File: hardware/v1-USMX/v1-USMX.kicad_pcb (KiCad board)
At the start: 2 copper layers, 91.4 x 48.8 mm, 38 parts, among them IC1 MAX98357AETE+T (L), IC2 MAX98357AETE+T (R), J1 +5v_POWER, J2 Conn_01x04, J3 10118192-0002LF, J4 Serial_Breakout, U1 ESP32-S3-WROOM-1, U2 AZ1084-3.3

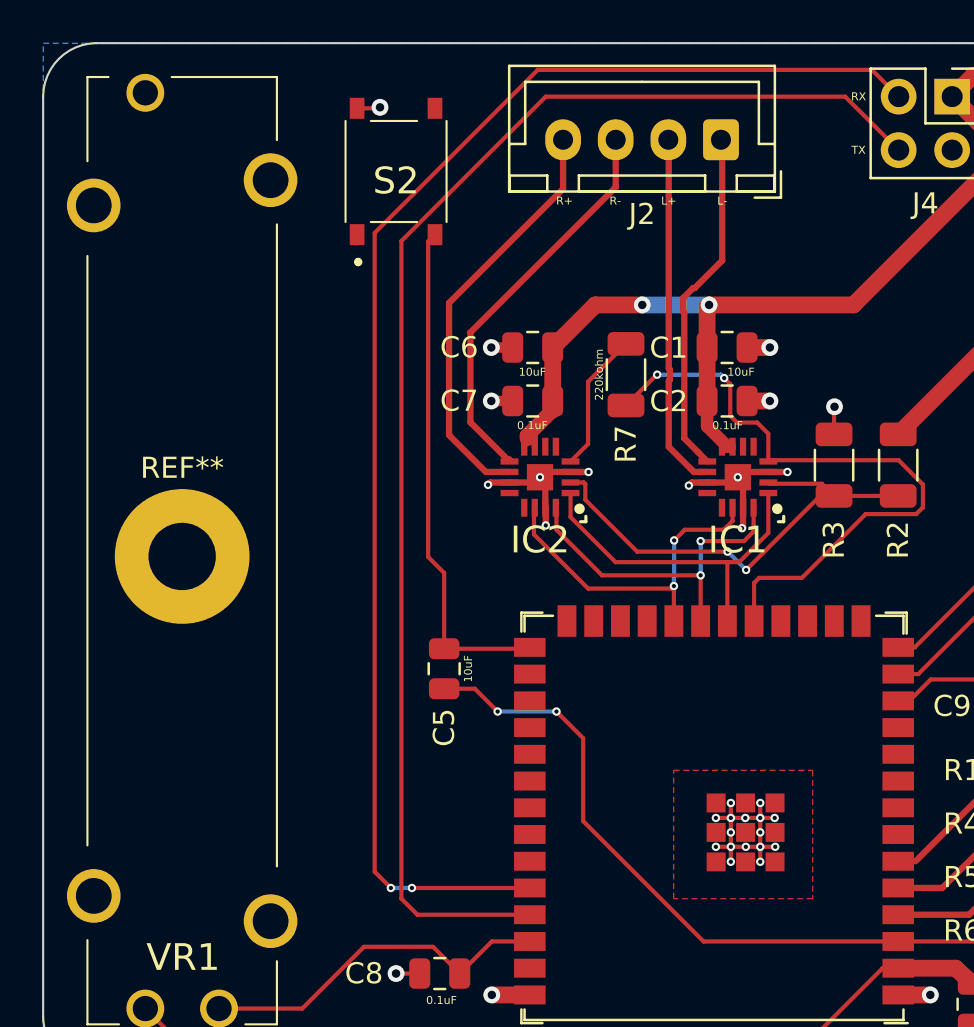
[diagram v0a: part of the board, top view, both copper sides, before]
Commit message: passes all DRC
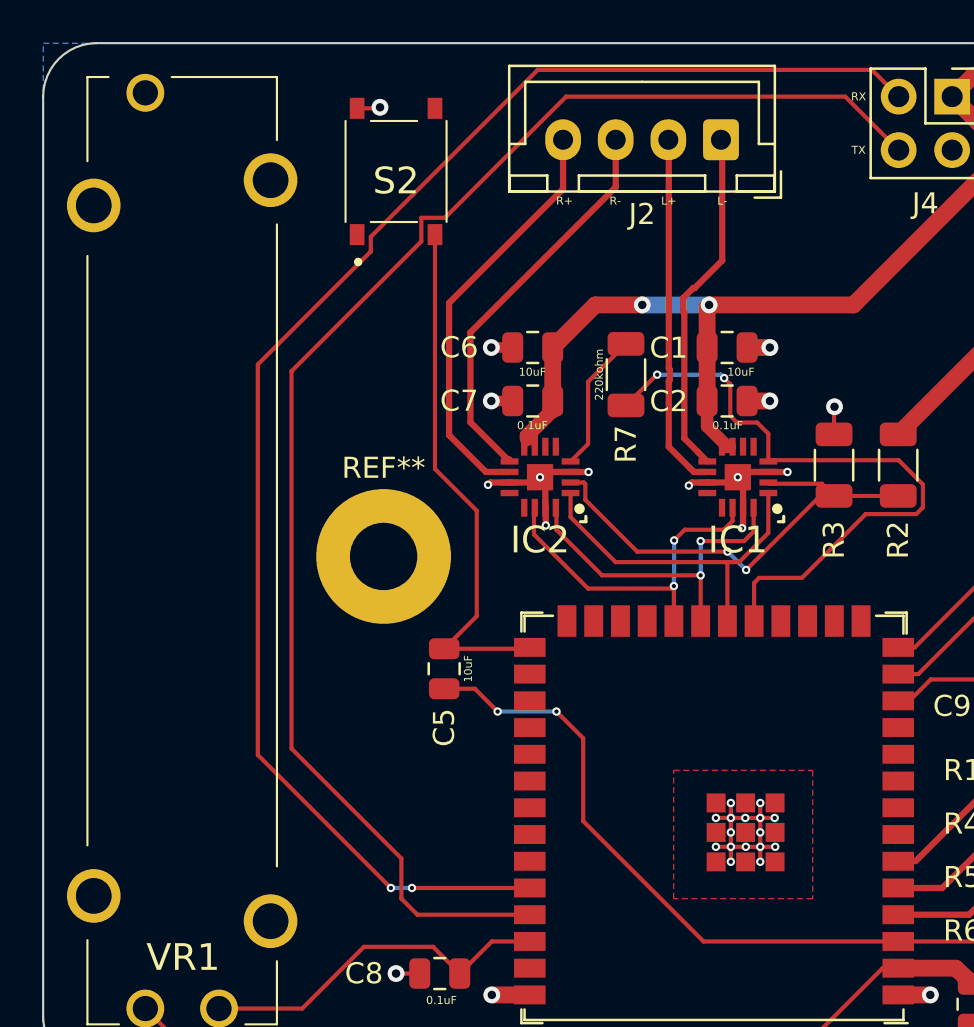
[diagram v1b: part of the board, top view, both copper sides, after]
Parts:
- moved REF** 9.57 mm to (114.7, 104.6)
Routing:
- net /U0RXD_TX: track 66.7 -> 71.3 mm
- net /U0TXD_RX: track 65.2 -> 69.6 mm
- net /RST_TO_PRGM: track 24.2 -> 25.2 mm
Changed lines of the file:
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@@
   )
   (footprint "MountingHole:MountingHole_3.2mm_M3_Pad" (layer "F.Cu")
-    (at 105.156 104.648)
+    (at 114.72472 104.648)
     (descr "Mounting Hole 3.2mm, M3")
     (tags "mounting hole 3.2mm m3")
@@
   (segment (start 146.780418 123.688418) (end 147.044 123.952) (width 0.2) (layer "B.Cu") (net 4))
   (segment (start 145.414918 123.688418) (end 146.780418 123.688418) (width 0.2) (layer "B.Cu") (net 4))
-  (segment (start 116.84 104.67) (end 117.602 105.432) (width 0.2) (layer "F.Cu") (net 7))
-  (segment (start 116.84 89.686) (end 116.84 104.67) (width 0.2) (layer "F.Cu") (net 7))
+  (segment (start 117.166 100.491) (end 119.15 102.475) (width 0.2) (layer "F.Cu") (net 7))
+  (segment (start 119.15 102.475) (end 119.15 107.484) (width 0.2) (layer "F.Cu") (net 7))
+  (segment (start 119.15 107.484) (end 117.602 109.032) (width 0.2) (layer "F.Cu") (net 7))
   (segment (start 117.602 109.032) (end 121.604 109.032) (width 0.2) (layer "F.Cu") (net 7))
-  (segment (start 117.602 105.432) (end 117.602 109.032) (width 0.2) (layer "F.Cu") (net 7))
-  (segment (start 117.166 89.36) (end 116.84 89.686) (width 0.2) (layer "F.Cu") (net 7))
+  (segment (start 117.166 89.36) (end 117.166 100.491) (width 0.2) (layer "F.Cu") (net 7))
   (segment (start 121.604 109.032) (end 121.67 108.966) (width 0.2) (layer "F.Cu") (net 7))
   (segment (start 140.12 110.236) (end 150.876 99.48) (width 0.2) (layer "F.Cu") (net 8))
@@
   (segment (start 123.25 84.853) (end 123.25 87.189) (width 0.3) (layer "F.Cu") (net 28))
   (segment (start 122.047 81.534) (end 137.922 81.534) (width 0.2) (layer "F.Cu") (net 34))
-  (segment (start 115.0705 120.396) (end 114.3 119.6255) (width 0.2) (layer "F.Cu") (net 34))
-  (segment (start 114.3 119.6255) (end 114.3 89.281) (width 0.2) (layer "F.Cu") (net 34))
+  (segment (start 108.75 114.0755) (end 108.75 95.526) (width 0.2) (layer "F.Cu") (net 34))
   (segment (start 137.922 81.534) (end 139.192 82.804) (width 0.2) (layer "F.Cu") (net 34))
-  (segment (start 114.3 89.281) (end 122.047 81.534) (width 0.2) (layer "F.Cu") (net 34))
+  (segment (start 115.0705 120.396) (end 108.75 114.0755) (width 0.2) (layer "F.Cu") (net 34))
+  (segment (start 114.116 90.16) (end 114.116 89.465) (width 0.2) (layer "F.Cu") (net 34))
+  (segment (start 108.75 95.526) (end 114.116 90.16) (width 0.2) (layer "F.Cu") (net 34))
+  (segment (start 114.116 89.465) (end 122.047 81.534) (width 0.2) (layer "F.Cu") (net 34))
   (segment (start 116.0695 120.396) (end 121.67 120.396) (width 0.2) (layer "F.Cu") (net 34))
   (via (at 116.0695 120.396) (size 0.4) (drill 0.2) (layers "F.Cu" "B.Cu") (net 34))
   (via (at 115.0705 120.396) (size 0.4) (drill 0.2) (layers "F.Cu" "B.Cu") (net 34))
   (segment (start 115.0705 120.396) (end 116.0695 120.396) (width 0.2) (layer "B.Cu") (net 34))
-  (segment (start 115.57 89.662) (end 115.57 120.904) (width 0.2) (layer "F.Cu") (net 35))
+  (segment (start 116.516 88.56) (end 116.516 89.684) (width 0.2) (layer "F.Cu") (net 35))
+  (segment (start 139.192 85.344) (end 136.652 82.804) (width 0.2) (layer "F.Cu") (net 35))
+  (segment (start 115.57 120.904) (end 116.332 121.666) (width 0.2) (layer "F.Cu") (net 35))
+  (segment (start 110.35 113.775) (end 115.57 118.995) (width 0.2) (layer "F.Cu") (net 35))
+  (segment (start 115.57 118.995) (end 115.57 120.904) (width 0.2) (layer "F.Cu") (net 35))
+  (segment (start 110.35 95.85) (end 110.35 113.775) (width 0.2) (layer "F.Cu") (net 35))
+  (segment (start 116.516 89.684) (end 110.35 95.85) (width 0.2) (layer "F.Cu") (net 35))
+  (segment (start 117.64 88.56) (end 116.516 88.56) (width 0.2) (layer "F.Cu") (net 35))
+  (segment (start 136.652 82.804) (end 123.396 82.804) (width 0.2) (layer "F.Cu") (net 35))
+  (segment (start 123.396 82.804) (end 117.64 88.56) (width 0.2) (layer "F.Cu") (net 35))
   (segment (start 116.332 121.666) (end 121.67 121.666) (width 0.2) (layer "F.Cu") (net 35))
-  (segment (start 136.652 82.804) (end 122.428 82.804) (width 0.2) (layer "F.Cu") (net 35))
-  (segment (start 122.428 82.804) (end 115.57 89.662) (width 0.2) (layer "F.Cu") (net 35))
-  (segment (start 115.57 120.904) (end 116.332 121.666) (width 0.2) (layer "F.Cu") (net 35))
-  (segment (start 139.192 85.344) (end 136.652 82.804) (width 0.2) (layer "F.Cu") (net 35))
   (segment (start 181.398 125.434) (end 181.398 124.956) (width 0.3) (layer "F.Cu") (net 36))
   (segment (start 146.324 118.221528) (end 146.675472 118.573) (width 0.3) (layer "F.Cu") (net 36))

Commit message: misc
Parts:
- moved S1 0.78 mm to (180.7, 86.4)
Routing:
- net /RESET: track 114.9 -> 114.2 mm
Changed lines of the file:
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@@
   )
   (footprint "my-footprints:PTS526SM08SMTR2LFS" (layer "F.Cu")
-    (at 180.733 85.598 90)
+    (at 180.675 86.375 90)
     (descr "PTS526 SM08 SMTR2 LFS-1")
     (tags "Switch")
@@
   (segment (start 132.6168 118.4402) (end 132.6168 117.7544) (width 0.2) (layer "F.Cu") (net 2))
   (segment (start 123.6068 100.6348) (end 123.606 100.634) (width 0.3) (layer "F.Cu") (net 2))
-  (segment (start 179.717 82.55) (end 178.931 82.55) (width 0.25) (layer "F.Cu") (net 2))
   (segment (start 153.904 82.5306) (end 153.904 84.3806) (width 0.8) (layer "F.Cu") (net 2))
   (segment (start 148.904 82.5306) (end 151.304 82.5306) (width 0.8) (layer "F.Cu") (net 2))
@@
   (segment (start 152.781 100.965) (end 153.99 100.965) (width 0.5) (layer "F.Cu") (net 2))
   (segment (start 120.706 101.134) (end 121.906 101.134) (width 0.3) (layer "F.Cu") (net 2))
+  (segment (start 178.888 83.312) (end 178.825 83.375) (width 0.25) (layer "F.Cu") (net 2))
   (segment (start 130.1 101.134) (end 131.3 101.134) (width 0.3) (layer "F.Cu") (net 2))
   (segment (start 154.6954 85.0806) (end 153.204 85.0806) (width 0.8) (layer "F.Cu") (net 2))
@@
   (segment (start 136.122 98.8475) (end 136.122 97.558) (width 0.2) (layer "F.Cu") (net 2))
   (segment (start 164.719 88.9) (end 163.449 88.9) (width 0.8) (layer "F.Cu") (net 2))
+  (segment (start 179.832 83.312) (end 178.888 83.312) (width 0.25) (layer "F.Cu") (net 2))
   (segment (start 131.2198 117.0686) (end 130.5086 117.0686) (width 0.2) (layer "F.Cu") (net 2))
   (segment (start 143.256 112.268) (end 143.83 112.268) (width 0.5) (layer "F.Cu") (net 2))
@@
   (via (at 145.266 127.95) (size 0.8) (drill 0.4) (layers "F.Cu" "B.Cu") (free) (net 2))
   (via (at 130.5086 117.0686) (size 0.4) (drill 0.2) (layers "F.Cu" "B.Cu") (free) (net 2))
-  (via (at 179.717 82.55) (size 0.8) (drill 0.4) (layers "F.Cu" "B.Cu") (free) (net 2))
+  (via (at 179.832 83.312) (size 0.8) (drill 0.4) (layers "F.Cu" "B.Cu") (free) (net 2))
   (via (at 131.2198 117.7544) (size 0.4) (drill 0.2) (layers "F.Cu" "B.Cu") (free) (net 2))
   (via (at 154.94 84.836) (size 0.8) (drill 0.4) (layers "F.Cu" "B.Cu") (free) (net 2))
@@
   (segment (start 145.52 114.046) (end 145.52 120.7115) (width 0.8) (layer "F.Cu") (net 3))
   (segment (start 119.06 110.932) (end 117.602 110.932) (width 0.2) (layer "F.Cu") (net 4))
+  (segment (start 181.864 126.492) (end 186.436 121.92) (width 0.2) (layer "F.Cu") (net 4))
+  (segment (start 183.388 90.238) (end 182.525 89.375) (width 0.2) (layer "F.Cu") (net 4))
   (segment (start 145.414918 123.531418) (end 144.3115 122.428) (width 0.2) (layer "F.Cu") (net 4))
+  (segment (start 183.388 111.252) (end 183.388 90.238) (width 0.2) (layer "F.Cu") (net 4))
+  (segment (start 186.436 114.3) (end 183.388 111.252) (width 0.2) (layer "F.Cu") (net 4))
+  (segment (start 186.436 121.92) (end 186.436 114.3) (width 0.2) (layer "F.Cu") (net 4))
   (segment (start 124.206 117.221) (end 129.921 122.936) (width 0.2) (layer "F.Cu") (net 4))
   (segment (start 143.8035 122.936) (end 144.3115 122.428) (width 0.2) (layer "F.Cu") (net 4))
+  (segment (start 147.044 123.952) (end 149.584 126.492) (width 0.2) (layer "F.Cu") (net 4))
   (segment (start 145.414918 123.688418) (end 145.414918 123.531418) (width 0.2) (layer "F.Cu") (net 4))
-  (segment (start 181.864 126.492) (end 186.436 121.92) (width 0.2) (layer "F.Cu") (net 4))
-  (segment (start 186.436 114.3) (end 183.388 111.252) (width 0.2) (layer "F.Cu") (net 4))
-  (segment (start 186.436 121.92) (end 186.436 114.3) (width 0.2) (layer "F.Cu") (net 4))
-  (segment (start 183.388 111.252) (end 183.388 89.403) (width 0.2) (layer "F.Cu") (net 4))
   (segment (start 120.142 112.014) (end 119.06 110.932) (width 0.2) (layer "F.Cu") (net 4))
   (segment (start 122.936 112.014) (end 124.206 113.284) (width 0.2) (layer "F.Cu") (net 4))
@@
   (segment (start 143.234 122.936) (end 143.8035 122.936) (width 0.2) (layer "F.Cu") (net 4))
   (segment (start 149.584 126.492) (end 181.864 126.492) (width 0.2) (layer "F.Cu") (net 4))
-  (segment (start 183.388 89.403) (end 182.583 88.598) (width 0.2) (layer "F.Cu") (net 4))
-  (segment (start 147.044 123.952) (end 149.584 126.492) (width 0.2) (layer "F.Cu") (net 4))
   (segment (start 139.17 122.936) (end 143.234 122.936) (width 0.2) (layer "F.Cu") (net 4))
   (segment (start 129.921 122.936) (end 139.17 122.936) (width 0.2) (layer "F.Cu") (net 4))

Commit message: misc
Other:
- board text added: "v1-PSMX.beta-1"
- board text removed: "v1-PSMX.test-1"
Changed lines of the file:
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@@
     (effects (font (size 0.381 0.381) (thickness 0.09525)))
   )
-  (gr_text "v1-PSMX.test-1" (at 180.975 127.889) (layer "F.SilkS")
+  (gr_text "v1-PSMX.beta-1" (at 180.975 127.889) (layer "F.SilkS")
     (effects (font (size 1 1) (thickness 0.15)))
   )

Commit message: Created Gerbers And Drill
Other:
- board text added: "v1-USMX.beta-1"
- board text removed: "v1-PSMX.beta-1"
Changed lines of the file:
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@@
     (effects (font (size 0.381 0.381) (thickness 0.09525)))
   )
-  (gr_text "v1-PSMX.beta-1" (at 180.975 127.889) (layer "F.SilkS")
+  (gr_text "v1-USMX.beta-1" (at 180.975 127.889) (layer "F.SilkS")
     (effects (font (size 1 1) (thickness 0.15)))
   )
